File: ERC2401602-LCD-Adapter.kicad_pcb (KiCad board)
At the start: 2 copper layers, 100 x 70 mm, 69 parts, among them J1 LCD ERC240160XX-2, J2 Backlight, J3 LCD Debug, J4 Backlight Debug, J5 Left, J6 Bottom, Q1 2N7002

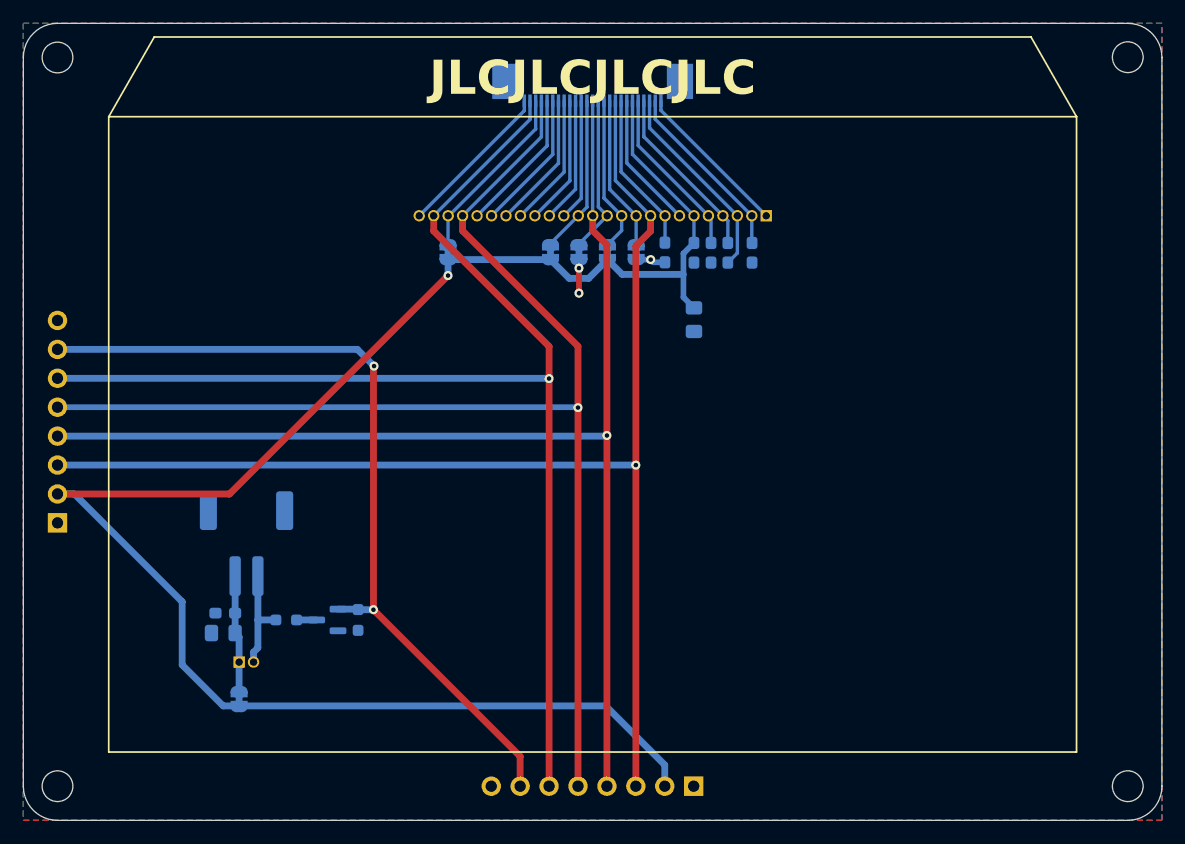
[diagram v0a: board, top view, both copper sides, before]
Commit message: Fixed Resistor and BG Polarity
- Changed the current limiting resistor value to 3.9R
- Fixed the Background Light connector Polarity
- Moved the LCD connector down 5mm
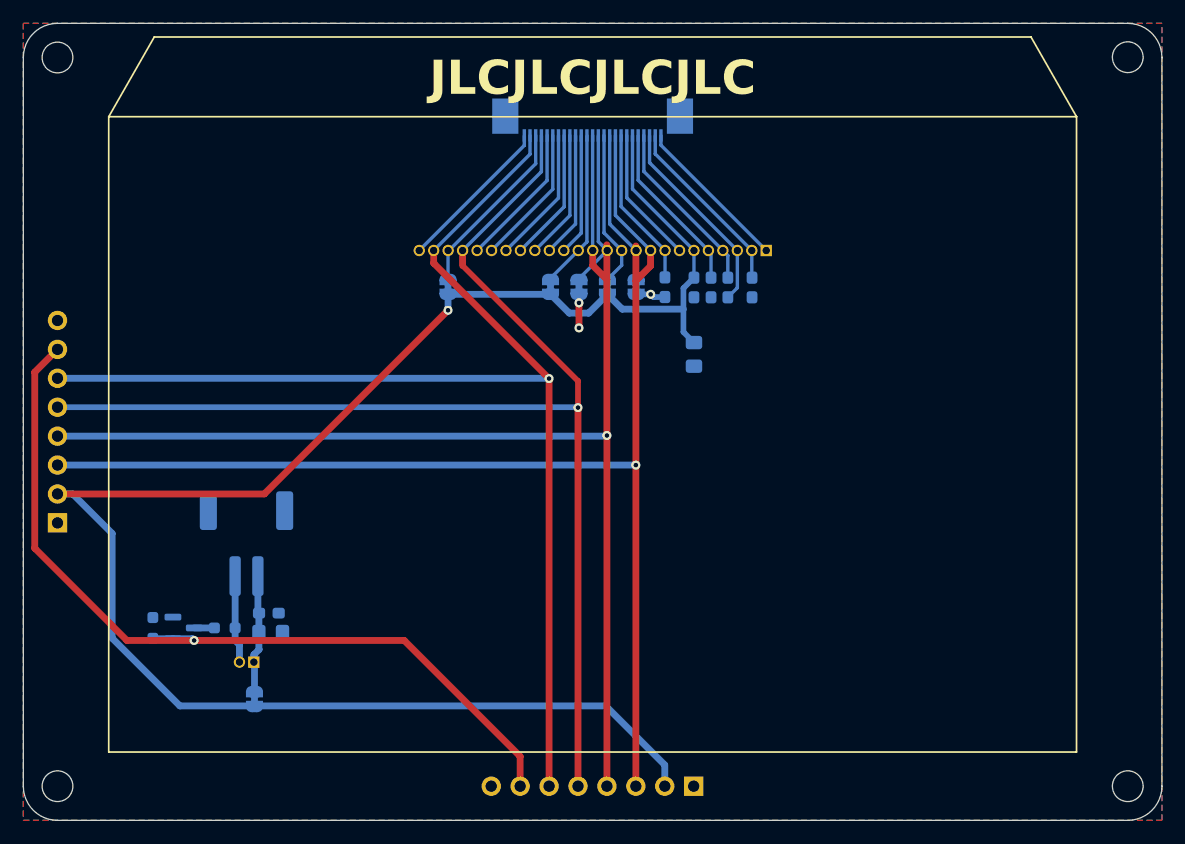
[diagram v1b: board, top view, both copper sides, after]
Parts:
- R2: value 20 -> 3.9R
- moved R1 18.0 mm to (103.9, 100.1), turned to 90 degrees
- moved Q1 12.6 mm to (106.6, 100.1), turned to 0 degrees
- moved R2 5.45 mm to (110.2, 100.1), turned to 180 degrees
- moved C7 4.16 mm to (114.2, 100.5), turned to 0 degrees
- moved C8 3.83 mm to (114.1, 98.8), turned to 0 degrees
- moved JP1 3.05 mm to (146.3, 70.2)
- moved JP2 3.05 mm to (143.8, 70.2)
- moved JP3 3.05 mm to (141.3, 70.2)
- moved JP4 3.05 mm to (138.8, 70.2)
- moved JP5 3.05 mm to (129.8, 70.2)
- moved J3 3.05 mm to (157.8, 67.0)
- moved kibuzzard-658C9D05 3.05 mm to (128.6, 64.2)
- moved kibuzzard-658C9D10 3.05 mm to (131.1, 64.2)
- moved kibuzzard-658C9D14 3.05 mm to (132.3, 64.2)
- moved kibuzzard-658C9D17 3.05 mm to (133.6, 64.2)
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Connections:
- J2 pad 1: BL_A -> BL_K
- J2 pad 2: BL_K -> BL_A
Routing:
- net D0: track 113.0 -> 109.9 mm
- net A0: track 111.1 -> 108.0 mm
- net BL_K: track 9.28 -> 7.71 mm
- net BL_CTRL: track 73.8 -> 74.8 mm, vias 2 -> 1
- net VDD: track 155.9 -> 156.8 mm
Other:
- board text added: "REV 1.1 - 2023-02-24"
- board text removed: "REV 1.0 - 2023-12-27"

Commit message: Added DC PIN
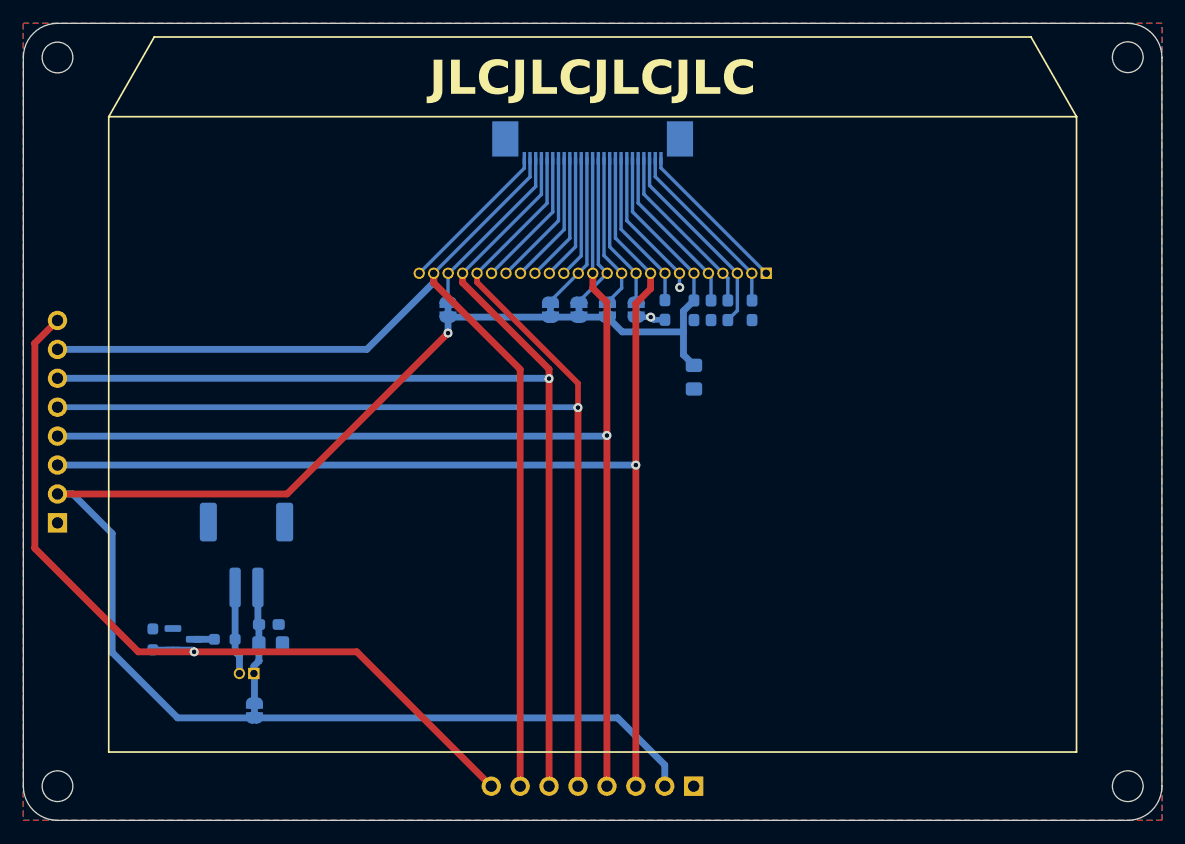
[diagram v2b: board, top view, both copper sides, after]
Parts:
- removed the kibuzzard-658C9B20 at (99.1, 73.1)
- removed the kibuzzard-658C9B20 at (133.6, 110.4)
- removed the kibuzzard-658C9B93 at (136.1, 110.8)
- added REF**: WEEE-Logo_4.2x6mm_SilkScreen, Symbol:WEEE-Logo_4.2x6mm_SilkScreen, B.Cu at (161.1, 105.8)
- added REF**: CE-Logo_8.5x6mm_SilkScreen, Symbol:CE-Logo_8.5x6mm_SilkScreen, B.Cu at (170.1, 105.8)
- added REF**: ESD-Logo_6.6x6mm_SilkScreen, Symbol:ESD-Logo_6.6x6mm_SilkScreen, B.Cu at (179.1, 105.8)
- added kibuzzard-663E4C56: G***, kibuzzard-663E4C56, B.Cu at (133.6, 110.8)
- added kibuzzard-663E4C9C: G***, kibuzzard-663E4C9C, B.Cu at (98.7, 80.7)
- added kibuzzard-663E4C9C: G***, kibuzzard-663E4C9C, B.Cu at (141.2, 110.8)
- moved kibuzzard-658C9B6D 2.60 mm to (99.1, 75.6)
- moved kibuzzard-658C9B5D 2.60 mm to (99.1, 78.2)
- moved kibuzzard-658C9B5D 2.55 mm to (138.7, 110.4)
- moved kibuzzard-658C9B6D 2.55 mm to (136.2, 110.4)
- moved kibuzzard-658C9B93 2.50 mm to (98.7, 73.1)
- moved C1 2.00 mm to (151.4, 72.2)
- moved C2 2.00 mm to (151.4, 78.1)
- moved C3 2.00 mm to (156.5, 72.2)
- moved C4 2.00 mm to (154.4, 72.2)
- moved C5 2.00 mm to (152.9, 72.2)
- moved C6 2.00 mm to (148.8, 72.2)
- moved J1 2.00 mm to (142.5, 57.5)
- moved J3 2.00 mm to (157.8, 69.0)
- moved JP1 2.00 mm to (146.3, 72.2)
- moved JP2 2.00 mm to (143.8, 72.2)
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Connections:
- J5 pad 5: D0 -> D1
- J5 pad 6: A0 -> D0
- J5 pad 7: BL_CTRL -> A0
- J5 pad 8: GND -> BL_CTRL
- J6 pad 5: D0 -> D1
- J6 pad 6: A0 -> D0
- J6 pad 7: BL_CTRL -> A0
- J6 pad 8: GND -> BL_CTRL
- JP3 pad 1: GND -> VDD
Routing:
- net D1: track 12.6 -> 107.1 mm, vias 0 -> 1
- net A0: track 108.0 -> 98.1 mm, vias 1 -> 0
- net D0: track 109.9 -> 104.4 mm
- net RST: track 109.0 -> 103.9 mm
- net CSB: track 112.8 -> 107.8 mm
- net GND: track 45.4 -> 43.8 mm, vias 3 -> 2
- net BL_CTRL: track 74.8 -> 73.3 mm
- net VDD: track 156.8 -> 155.3 mm
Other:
- board text added: "ERC240160 LCD Adapter Board"
- board text added: "REV 1.3 - 2024-05-10"
- board text removed: "A, A"
- board text removed: "ERC240160-2 LCD Adapter Board"
- board text removed: "Holes"
- board text removed: "LCD"
- board text removed: "LCD & BL"
- board text removed: "PCB"
- board text removed: "REV 1.1 - 2023-02-24"
- board text removed: "V, A"
